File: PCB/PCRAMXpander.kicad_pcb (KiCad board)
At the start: 2 copper layers, 134.6 x 97.8 mm, 22 parts, among them J1 Bus_ISA_16bit, U1 ATF16V8B-15PU, U2 SN74LVCR16245ADGGR, U3 SN74LVC16244ADGGR, U4 SN74LVC16244ADGGR, U5 AS6C3216A-55TIN, U6 AS6C3216A-55TIN

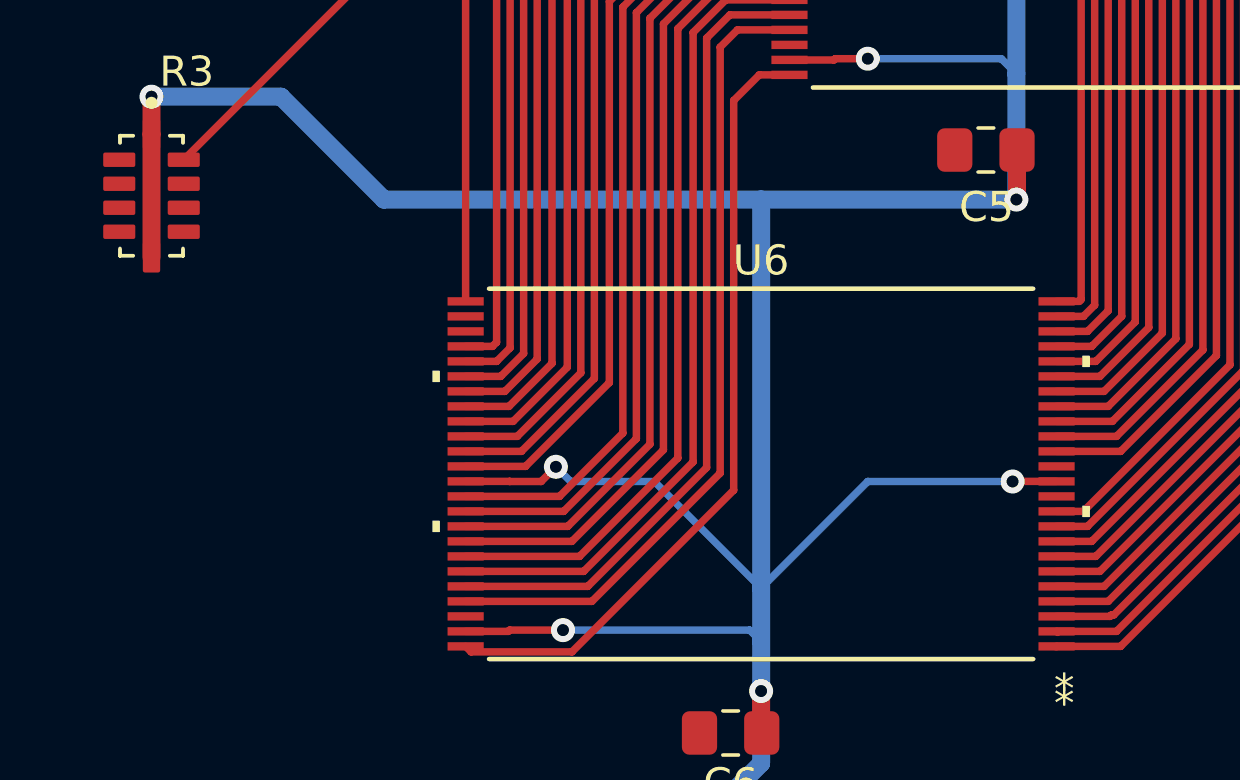
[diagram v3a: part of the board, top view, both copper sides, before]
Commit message: More manual routing
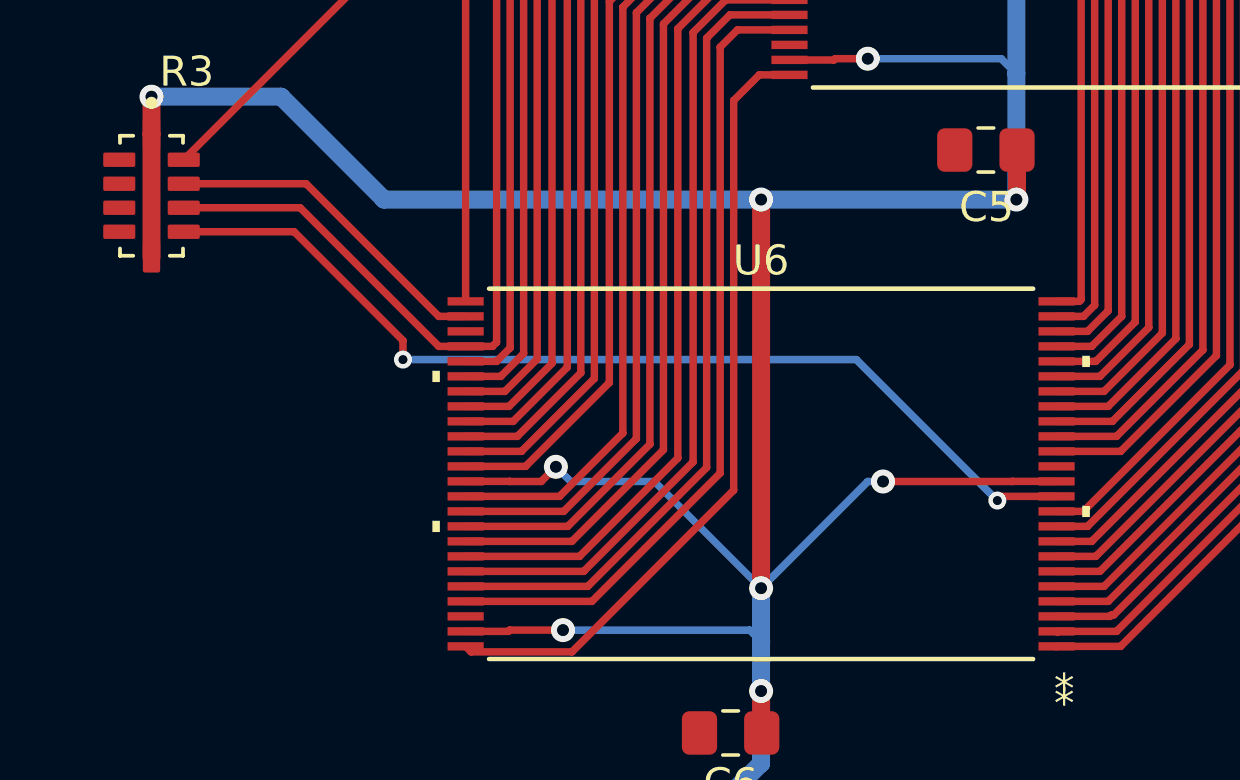
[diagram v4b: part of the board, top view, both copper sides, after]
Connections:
- R3 pad 7: C2E -> WE
- R3 pad 9: WE -> C2E
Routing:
- net WE: track 0.00 -> 33.2 mm, vias 0 -> 2
- net OE: track 26.1 -> 37.4 mm
- net C2E: track 0.00 -> 11.2 mm
- net +3.3V: vias 13 -> 15
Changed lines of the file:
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@@
 			(layers "F.Cu" "F.Mask" "F.Paste")
 			(roundrect_rratio 0.125)
-			(net 98 "C2E")
+			(net 99 "WE")
 			(pintype "passive")
 			(solder_mask_margin 0.102)
@@
 			(layers "F.Cu" "F.Mask" "F.Paste")
 			(roundrect_rratio 0.125)
-			(net 99 "WE")
+			(net 98 "C2E")
 			(pintype "passive")
 			(solder_mask_margin 0.102)
@@
 	)
 	(segment
+		(start 122.995 74.695)
+		(end 126.875201 74.695)
+		(width 0.25)
+		(layer "F.Cu")
+		(net 96)
+	)
+	(segment
+		(start 131.496202 79.316001)
+		(end 132.39115 79.316001)
+		(width 0.25)
+		(layer "F.Cu")
+		(net 96)
+	)
+	(segment
+		(start 126.875201 74.695)
+		(end 131.496202 79.316001)
+		(width 0.25)
+		(layer "F.Cu")
+		(net 96)
+	)
+	(segment
 		(start 132.39115 79.316001)
 		(end 133.286098 79.316001)
@@
 	)
 	(segment
+		(start 127.075199 73.895)
+		(end 131.496199 78.316)
+		(width 0.25)
+		(layer "F.Cu")
+		(net 98)
+	)
+	(segment
+		(start 122.995 73.895)
+		(end 127.075199 73.895)
+		(width 0.25)
+		(layer "F.Cu")
+		(net 98)
+	)
+	(segment
+		(start 131.496199 78.316)
+		(end 132.39115 78.316)
+		(width 0.25)
+		(layer "F.Cu")
+		(net 98)
+	)
+	(segment
+		(start 150.252999 84.316001)
+		(end 152.08885 84.316001)
+		(width 0.25)
+		(layer "F.Cu")
+		(net 99)
+	)
+	(segment
+		(start 126.676 75.495)
+		(end 130.302 79.121)
+		(width 0.25)
+		(layer "F.Cu")
+		(net 99)
+	)
+	(segment
+		(start 130.302 79.121)
+		(end 130.302 79.756)
+		(width 0.25)
+		(layer "F.Cu")
+		(net 99)
+	)
+	(segment
+		(start 122.995 75.495)
+		(end 126.676 75.495)
+		(width 0.25)
+		(layer "F.Cu")
+		(net 99)
+	)
+	(segment
+		(start 150.114 84.455)
+		(end 150.252999 84.316001)
+		(width 0.25)
+		(layer "F.Cu")
+		(net 99)
+	)
+	(via
+		(at 130.302 79.756)
+		(size 0.6)
+		(drill 0.3)
+		(layers "F.Cu" "B.Cu")
+		(net 99)
+	)
+	(via
+		(at 150.114 84.455)
+		(size 0.6)
+		(drill 0.3)
+		(layers "F.Cu" "B.Cu")
+		(net 99)
+	)
+	(segment
+		(start 145.415 79.756)
+		(end 150.114 84.455)
+		(width 0.25)
+		(layer "B.Cu")
+		(net 99)
+	)
+	(segment
+		(start 130.302 79.756)
+		(end 145.415 79.756)
+		(width 0.25)
+		(layer "B.Cu")
+		(net 99)
+	)
+	(segment
 		(start 110.582 107.606)
 		(end 92.588001 107.606)
@@
 	)
 	(segment
+		(start 150.622 83.82)
+		(end 150.626 83.816)
+		(width 0.25)
+		(layer "F.Cu")
+		(net 153)
+	)
+	(segment
 		(start 151.253498 122.380999)
 		(end 153.797499 124.925)
@@
 	)
 	(segment
+		(start 142.24 74.422)
+		(end 142.24 87.376)
+		(width 0.6)
+		(layer "F.Cu")
+		(net 153)
+	)
+	(segment
 		(start 156.7535 122.4205)
 		(end 159.258 124.925)
@@
 	)
 	(segment
+		(start 146.304 83.82)
+		(end 150.622 83.82)
+		(width 0.25)
+		(layer "F.Cu")
+		(net 153)
+	)
+	(segment
 		(start 161.47815 64.77)
 		(end 162.941 64.77)
@@
 	)
 	(segment
+		(start 150.626 83.816)
+		(end 152.08885 83.816)
+		(width 0.25)
+		(layer "F.Cu")
+		(net 153)
+	)
+	(segment
 		(start 116.7345 125.984)
 		(end 113.1355 125.984)
@@
 	)
 	(segment
-		(start 152.08885 83.816)
-		(end 150.626 83.816)
-		(width 0.25)
-		(layer "F.Cu")
-		(net 153)
-	)
-	(segment
 		(start 106.426 103.9075)
 		(end 116.250002 103.9075)
@@
 	)
 	(segment
-		(start 150.626 83.816)
-		(end 150.622 83.82)
-		(width 0.25)
-		(layer "F.Cu")
-		(net 153)
-	)
-	(segment
 		(start 142.24 90.805)
 		(end 142.24 92.1805)
@@
 	)
 	(via
+		(at 142.24 74.422)
+		(size 0.8)
+		(drill 0.4)
+		(layers "F.Cu" "B.Cu")
+		(net 153)
+	)
+	(via
 		(at 150.749 74.422)
 		(size 0.8)
@@
 	)
 	(via
-		(at 150.622 83.82)
+		(at 146.304 83.82)
 		(size 0.8)
 		(drill 0.4)
@@
 	)
 	(via
+		(at 142.24 87.376)
+		(size 0.8)
+		(drill 0.4)
+		(layers "F.Cu" "B.Cu")
+		(net 153)
+	)
+	(via
 		(at 145.796 69.727)
 		(size 0.8)
@@
 	)
 	(segment
-		(start 150.622 83.82)
+		(start 146.304 83.82)
 		(end 145.796 83.82)
 		(width 0.25)
@@
 	)
 	(segment
+		(start 150.749 74.422)
+		(end 142.24 74.422)
+		(width 0.6)
+		(layer "B.Cu")
+		(net 153)
+	)
+	(segment
+		(start 145.796 83.82)
+		(end 142.24 87.376)
+		(width 0.25)
+		(layer "B.Cu")
+		(net 153)
+	)
+	(segment
 		(start 135.399941 83.329943)
 		(end 135.889998 83.82)
@@
 	)
 	(segment
-		(start 126.238 70.993)
-		(end 121.92 70.993)
-		(width 0.6)
-		(layer "B.Cu")
-		(net 153)
-	)
-	(segment
 		(start 145.796 69.727)
 		(end 150.245 69.727)
@@
 	)
 	(segment
-		(start 87.8744 118.618)
-		(end 106.299 118.618)
+		(start 142.24 74.422)
+		(end 129.667 74.422)
 		(width 0.6)
 		(layer "B.Cu")
@@
 	)
 	(segment
-		(start 106.299 118.618)
-		(end 136.144 118.618)
+		(start 87.8744 118.618)
+		(end 106.299 118.618)
 		(width 0.6)
 		(layer "B.Cu")
@@
 	)
 	(segment
-		(start 145.796 83.82)
-		(end 142.24 87.376)
-		(width 0.25)
+		(start 106.299 118.618)
+		(end 136.144 118.618)
+		(width 0.6)
 		(layer "B.Cu")
 		(net 153)
 	)
 	(segment
-		(start 142.24 74.422)
-		(end 142.24 87.376)
+		(start 126.238 70.993)
+		(end 121.92 70.993)
 		(width 0.6)
 		(layer "B.Cu")
@@
 	)
 	(segment
-		(start 129.667 74.422)
-		(end 126.238 70.993)
-		(width 0.6)
-		(layer "B.Cu")
-		(net 153)
-	)
-	(segment
 		(start 142.24 93.218)
 		(end 142.24 90.805)
@@
 	)
 	(segment
-		(start 142.24 74.422)
-		(end 129.667 74.422)
-		(width 0.6)
-		(layer "B.Cu")
-		(net 153)
-	)
-	(segment
 		(start 150.749 70.231)
 		(end 150.749 67.78605)
@@
 	)
 	(segment
-		(start 150.749 74.422)
-		(end 142.24 74.422)
-		(width 0.6)
-		(layer "B.Cu")
-		(net 153)
-	)
-	(segment
 		(start 142.24 87.376)
 		(end 142.24 89.154)
@@
 		(layer "B.Cu")
 		(net 153)
+	)
+	(segment
+		(start 129.667 74.422)
+		(end 126.238 70.993)
+		(width 0.6)
+		(layer "B.Cu")
+		(net 153)

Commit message: More manual routing
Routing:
- net LA21: track 25.5 -> 74.7 mm, vias 0 -> 4
- net LA20: track 27.0 -> 72.9 mm, vias 2 -> 5
- net CS_HI: track 0.00 -> 38.6 mm, vias 0 -> 3
- net CS_LO: track 0.00 -> 37.1 mm, vias 0 -> 2
- net A15: track 24.8 -> 60.4 mm, vias 0 -> 2
- net BA00: track 0.00 -> 28.5 mm, vias 0 -> 2
- net LA22: track 74.8 -> 76.2 mm, vias 2 -> 3
- net LA23: track 80.4 -> 81.1 mm

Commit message: Revert "More manual routing"
This reverts commit b921debae46f28068d9de22bc133656cc87b6f20.
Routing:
- net LA21: track 74.7 -> 25.5 mm, vias 4 -> 0
- net LA20: track 72.9 -> 27.0 mm, vias 5 -> 2
- net CS_HI: track 38.6 -> 0.00 mm, vias 3 -> 0
- net CS_LO: track 37.1 -> 0.00 mm, vias 2 -> 0
- net A15: track 60.4 -> 24.8 mm, vias 2 -> 0
- net BA00: track 28.5 -> 0.00 mm, vias 2 -> 0
- net LA22: track 76.2 -> 74.8 mm, vias 3 -> 2
- net LA23: track 81.1 -> 80.4 mm

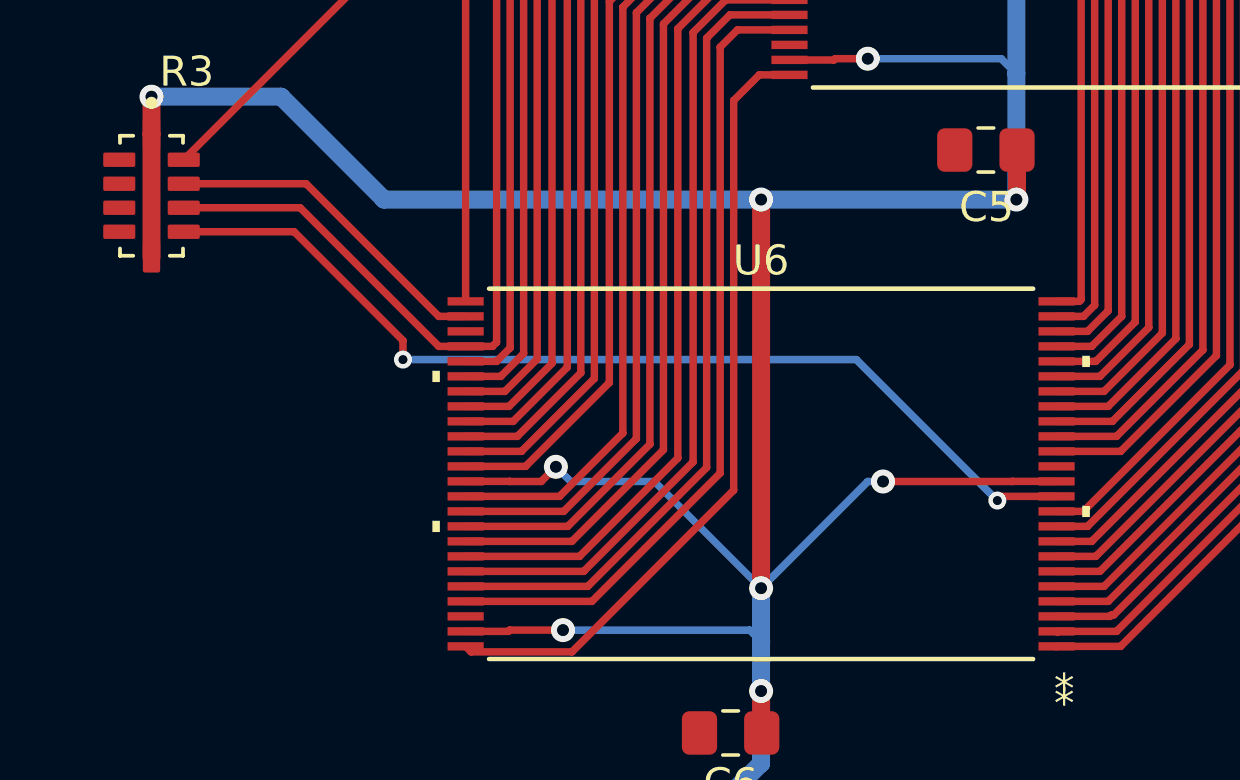
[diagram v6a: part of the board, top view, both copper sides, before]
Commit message: Revert "More manual routing"
This reverts commit 47449c23b7240c85fd4465f78316c60ac3030f38.
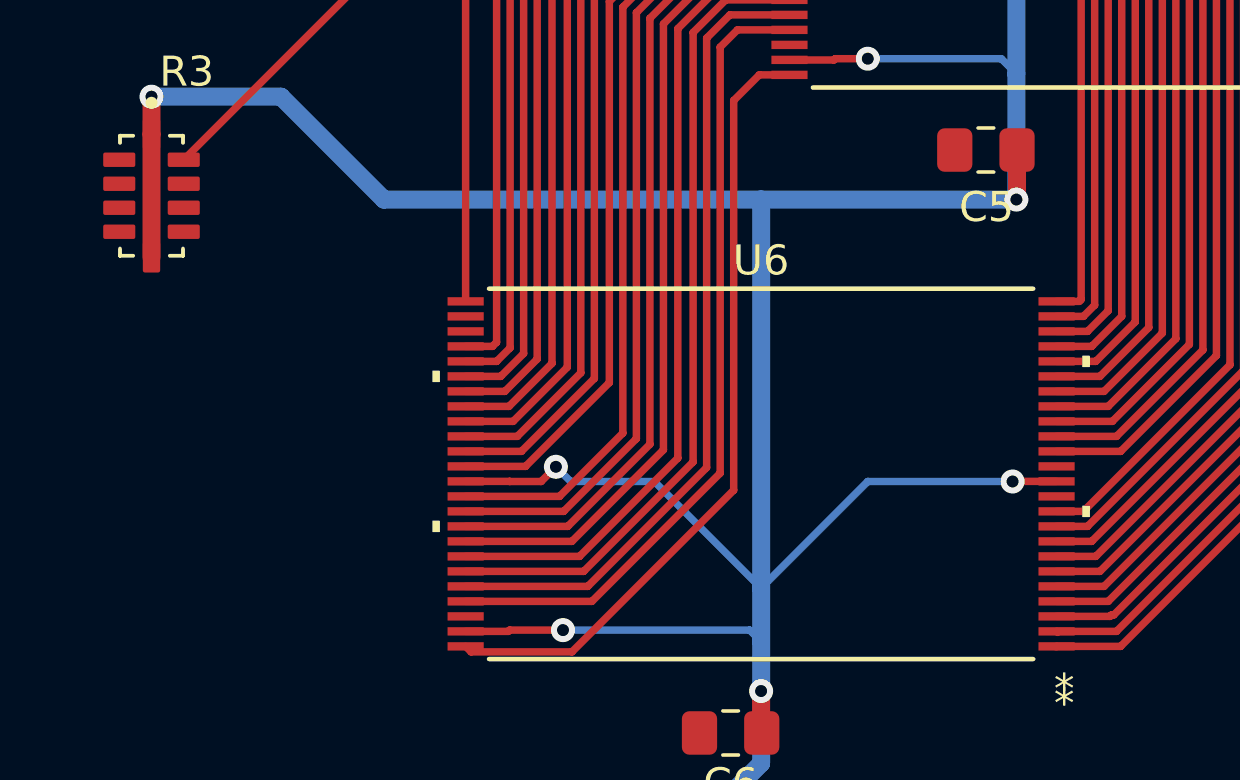
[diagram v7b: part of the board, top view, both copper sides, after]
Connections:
- R3 pad 7: WE -> C2E
- R3 pad 9: C2E -> WE
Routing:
- net WE: track 33.2 -> 0.00 mm, vias 2 -> 0
- net OE: track 37.4 -> 26.1 mm
- net C2E: track 11.2 -> 0.00 mm
- net +3.3V: vias 15 -> 13
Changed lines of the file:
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@@
 			(layers "F.Cu" "F.Mask" "F.Paste")
 			(roundrect_rratio 0.125)
-			(net 99 "WE")
+			(net 98 "C2E")
 			(pintype "passive")
 			(solder_mask_margin 0.102)
@@
 			(layers "F.Cu" "F.Mask" "F.Paste")
 			(roundrect_rratio 0.125)
-			(net 98 "C2E")
+			(net 99 "WE")
 			(pintype "passive")
 			(solder_mask_margin 0.102)
@@
 	)
 	(segment
-		(start 122.995 74.695)
-		(end 126.875201 74.695)
-		(width 0.25)
-		(layer "F.Cu")
-		(net 96)
-	)
-	(segment
-		(start 131.496202 79.316001)
-		(end 132.39115 79.316001)
-		(width 0.25)
-		(layer "F.Cu")
-		(net 96)
-	)
-	(segment
-		(start 126.875201 74.695)
-		(end 131.496202 79.316001)
-		(width 0.25)
-		(layer "F.Cu")
-		(net 96)
-	)
-	(segment
 		(start 132.39115 79.316001)
 		(end 133.286098 79.316001)
@@
 	)
 	(segment
-		(start 127.075199 73.895)
-		(end 131.496199 78.316)
-		(width 0.25)
-		(layer "F.Cu")
-		(net 98)
-	)
-	(segment
-		(start 122.995 73.895)
-		(end 127.075199 73.895)
-		(width 0.25)
-		(layer "F.Cu")
-		(net 98)
-	)
-	(segment
-		(start 131.496199 78.316)
-		(end 132.39115 78.316)
-		(width 0.25)
-		(layer "F.Cu")
-		(net 98)
-	)
-	(segment
-		(start 150.252999 84.316001)
-		(end 152.08885 84.316001)
-		(width 0.25)
-		(layer "F.Cu")
-		(net 99)
-	)
-	(segment
-		(start 126.676 75.495)
-		(end 130.302 79.121)
-		(width 0.25)
-		(layer "F.Cu")
-		(net 99)
-	)
-	(segment
-		(start 130.302 79.121)
-		(end 130.302 79.756)
-		(width 0.25)
-		(layer "F.Cu")
-		(net 99)
-	)
-	(segment
-		(start 122.995 75.495)
-		(end 126.676 75.495)
-		(width 0.25)
-		(layer "F.Cu")
-		(net 99)
-	)
-	(segment
-		(start 150.114 84.455)
-		(end 150.252999 84.316001)
-		(width 0.25)
-		(layer "F.Cu")
-		(net 99)
-	)
-	(via
-		(at 130.302 79.756)
-		(size 0.6)
-		(drill 0.3)
-		(layers "F.Cu" "B.Cu")
-		(net 99)
-	)
-	(via
-		(at 150.114 84.455)
-		(size 0.6)
-		(drill 0.3)
-		(layers "F.Cu" "B.Cu")
-		(net 99)
-	)
-	(segment
-		(start 145.415 79.756)
-		(end 150.114 84.455)
-		(width 0.25)
-		(layer "B.Cu")
-		(net 99)
-	)
-	(segment
-		(start 130.302 79.756)
-		(end 145.415 79.756)
-		(width 0.25)
-		(layer "B.Cu")
-		(net 99)
-	)
-	(segment
 		(start 110.582 107.606)
 		(end 92.588001 107.606)
@@
 	)
 	(segment
-		(start 150.622 83.82)
-		(end 150.626 83.816)
-		(width 0.25)
-		(layer "F.Cu")
-		(net 153)
-	)
-	(segment
 		(start 151.253498 122.380999)
 		(end 153.797499 124.925)
@@
 	)
 	(segment
-		(start 142.24 74.422)
-		(end 142.24 87.376)
-		(width 0.6)
-		(layer "F.Cu")
-		(net 153)
-	)
-	(segment
 		(start 156.7535 122.4205)
 		(end 159.258 124.925)
@@
 	)
 	(segment
-		(start 146.304 83.82)
-		(end 150.622 83.82)
-		(width 0.25)
-		(layer "F.Cu")
-		(net 153)
-	)
-	(segment
 		(start 161.47815 64.77)
 		(end 162.941 64.77)
@@
 	)
 	(segment
-		(start 150.626 83.816)
-		(end 152.08885 83.816)
-		(width 0.25)
-		(layer "F.Cu")
-		(net 153)
-	)
-	(segment
 		(start 116.7345 125.984)
 		(end 113.1355 125.984)
@@
 	)
 	(segment
+		(start 152.08885 83.816)
+		(end 150.626 83.816)
+		(width 0.25)
+		(layer "F.Cu")
+		(net 153)
+	)
+	(segment
 		(start 106.426 103.9075)
 		(end 116.250002 103.9075)
@@
 	)
 	(segment
+		(start 150.626 83.816)
+		(end 150.622 83.82)
+		(width 0.25)
+		(layer "F.Cu")
+		(net 153)
+	)
+	(segment
 		(start 142.24 90.805)
 		(end 142.24 92.1805)
@@
 	)
 	(via
-		(at 142.24 74.422)
-		(size 0.8)
-		(drill 0.4)
-		(layers "F.Cu" "B.Cu")
-		(net 153)
-	)
-	(via
 		(at 150.749 74.422)
 		(size 0.8)
@@
 	)
 	(via
-		(at 146.304 83.82)
+		(at 150.622 83.82)
 		(size 0.8)
 		(drill 0.4)
@@
 	)
 	(via
-		(at 142.24 87.376)
-		(size 0.8)
-		(drill 0.4)
-		(layers "F.Cu" "B.Cu")
-		(net 153)
-	)
-	(via
 		(at 145.796 69.727)
 		(size 0.8)
@@
 	)
 	(segment
-		(start 146.304 83.82)
+		(start 150.622 83.82)
 		(end 145.796 83.82)
 		(width 0.25)
@@
 	)
 	(segment
-		(start 150.749 74.422)
-		(end 142.24 74.422)
-		(width 0.6)
-		(layer "B.Cu")
-		(net 153)
-	)
-	(segment
-		(start 145.796 83.82)
-		(end 142.24 87.376)
-		(width 0.25)
-		(layer "B.Cu")
-		(net 153)
-	)
-	(segment
 		(start 135.399941 83.329943)
 		(end 135.889998 83.82)
@@
 	)
 	(segment
+		(start 126.238 70.993)
+		(end 121.92 70.993)
+		(width 0.6)
+		(layer "B.Cu")
+		(net 153)
+	)
+	(segment
 		(start 145.796 69.727)
 		(end 150.245 69.727)
@@
 	)
 	(segment
-		(start 142.24 74.422)
-		(end 129.667 74.422)
-		(width 0.6)
-		(layer "B.Cu")
-		(net 153)
-	)
-	(segment
 		(start 87.8744 118.618)
 		(end 106.299 118.618)
@@
 	)
 	(segment
-		(start 126.238 70.993)
-		(end 121.92 70.993)
+		(start 145.796 83.82)
+		(end 142.24 87.376)
+		(width 0.25)
+		(layer "B.Cu")
+		(net 153)
+	)
+	(segment
+		(start 142.24 74.422)
+		(end 142.24 87.376)
 		(width 0.6)
 		(layer "B.Cu")
@@
 	)
 	(segment
+		(start 129.667 74.422)
+		(end 126.238 70.993)
+		(width 0.6)
+		(layer "B.Cu")
+		(net 153)
+	)
+	(segment
 		(start 142.24 93.218)
 		(end 142.24 90.805)
@@
 	)
 	(segment
+		(start 142.24 74.422)
+		(end 129.667 74.422)
+		(width 0.6)
+		(layer "B.Cu")
+		(net 153)
+	)
+	(segment
 		(start 150.749 70.231)
 		(end 150.749 67.78605)
@@
 	)
 	(segment
+		(start 150.749 74.422)
+		(end 142.24 74.422)
+		(width 0.6)
+		(layer "B.Cu")
+		(net 153)
+	)
+	(segment
 		(start 142.24 87.376)
 		(end 142.24 89.154)
@@
 		(layer "B.Cu")
 		(net 153)
-	)
-	(segment
-		(start 129.667 74.422)
-		(end 126.238 70.993)
-		(width 0.6)
-		(layer "B.Cu")
-		(net 153)

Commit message: 5V done
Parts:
- moved C1 6.51 mm to (85.1, 86.4)
- moved C8 1.02 mm to (81.9, 124.5)
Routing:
- net +3.3V: track 378.2 -> 15.0 mm, vias 13 -> 0
- net Net-(J1-DB7): track 114.3 -> 6.99 mm
- net Net-(J1-DB4): track 111.9 -> 6.99 mm, vias 2 -> 0
- net Net-(J1-DB6): track 111.7 -> 6.99 mm, vias 2 -> 0
- net Net-(JP3-A): track 101.8 -> 0.00 mm, vias 2 -> 0
- net Net-(J1-DB5): track 108.5 -> 6.99 mm, vias 2 -> 0
- net Net-(J1-DB3): track 103.0 -> 6.99 mm, vias 2 -> 0
- net Net-(J1-DB2): track 100.3 -> 6.99 mm, vias 2 -> 0
- net Net-(J1-DB0): track 94.7 -> 6.99 mm, vias 2 -> 0
- net Net-(J1-DB1): track 92.7 -> 6.99 mm, vias 2 -> 0
- net LA23: track 80.4 -> 0.00 mm, vias 2 -> 0
- net LA22: track 74.8 -> 0.00 mm, vias 2 -> 0
- net Net-(J1-D15): track 64.8 -> 0.00 mm
- net Net-(J1-D14): track 62.7 -> 0.00 mm
- net Net-(J1-D13): track 61.1 -> 0.00 mm
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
